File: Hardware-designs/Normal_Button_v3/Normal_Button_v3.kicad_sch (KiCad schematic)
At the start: 40 parts, among them J1 UART, J2 Bat, J3 USB_C, Q1 MMBT3904, SW1 main, SW2 Aux, SW3 Side 1, SW4 Side 2, U1 ESP32-WROOM-32, U2 TP4057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

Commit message: Add pcb images, step file, and pdf schematic for all hardware designs.
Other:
- title: (none) -> HueMix-Link Normal Button
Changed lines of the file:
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@@
 	(generator_version "9.0")
 	(paper "A4")
+	(title_block
+		(title "HueMix-Link Normal Button")
+		(date "2026-02-18")
+		(rev "3.0")
+	)
 	(junction
 		(at 187.96 26.67)

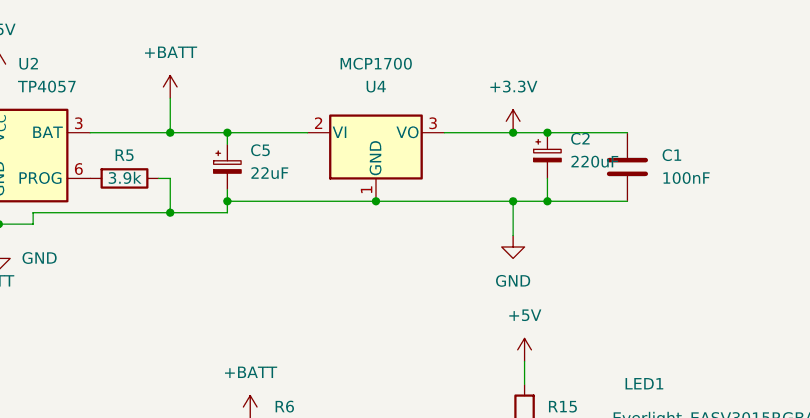
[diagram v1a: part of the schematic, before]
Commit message: correction voltage regulator
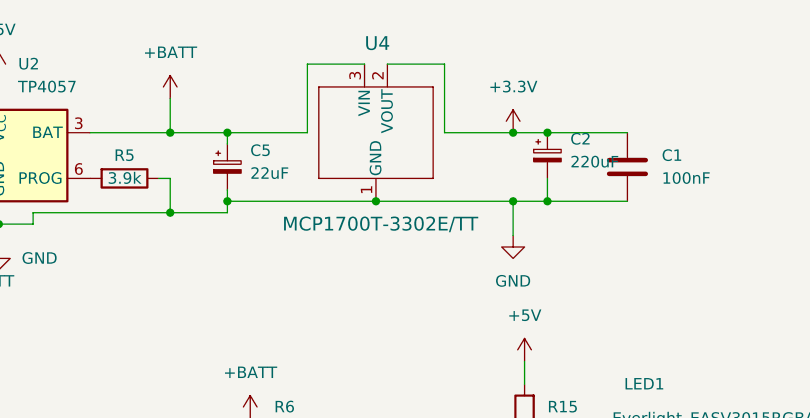
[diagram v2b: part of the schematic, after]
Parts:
- removed U4: MCP1700, MCP1700T_3302E_TT 3:SOT-23_MC_MCH, symbol Regulator_Linear:MCP1700-3302E_TO92
- added U4: MCP1700T-3302E/TT, SOT-23_MC_MCH, symbol 2025-12-22_17-16-21:MCP1700T-3302E_TT
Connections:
- net +3.3V: now also U4.2 (VOUT)
- net +BATT: now also U4.3 (VIN)
- net GND: now also U4.1 (GND)

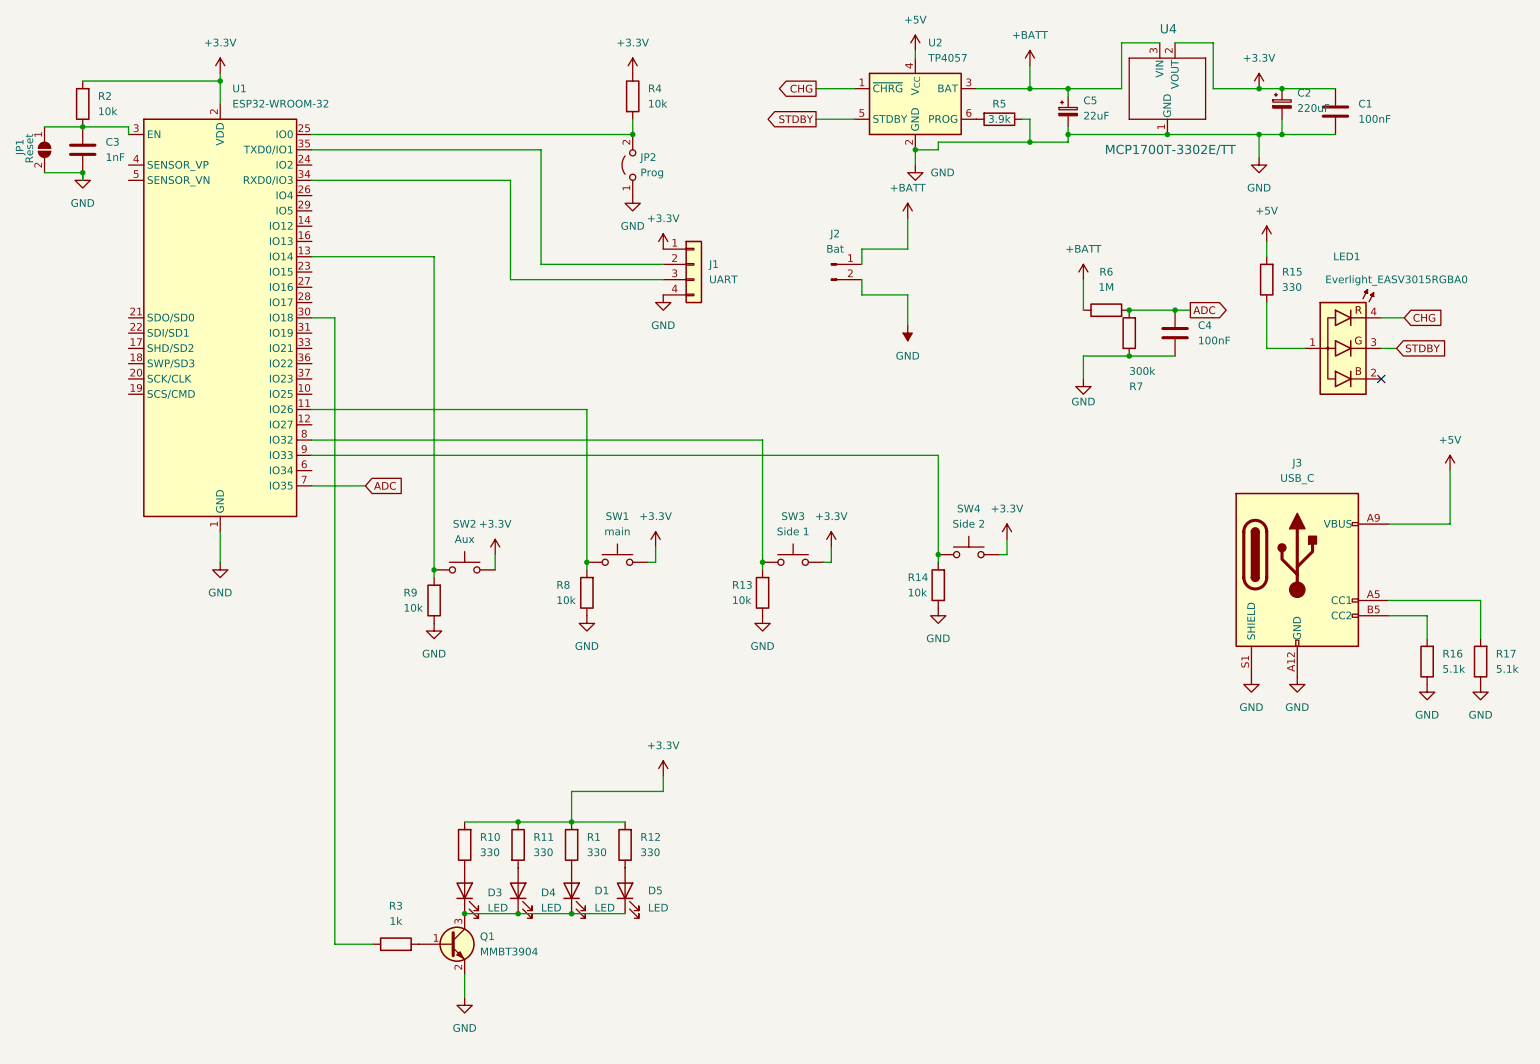
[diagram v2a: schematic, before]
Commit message: correction voltage regulator
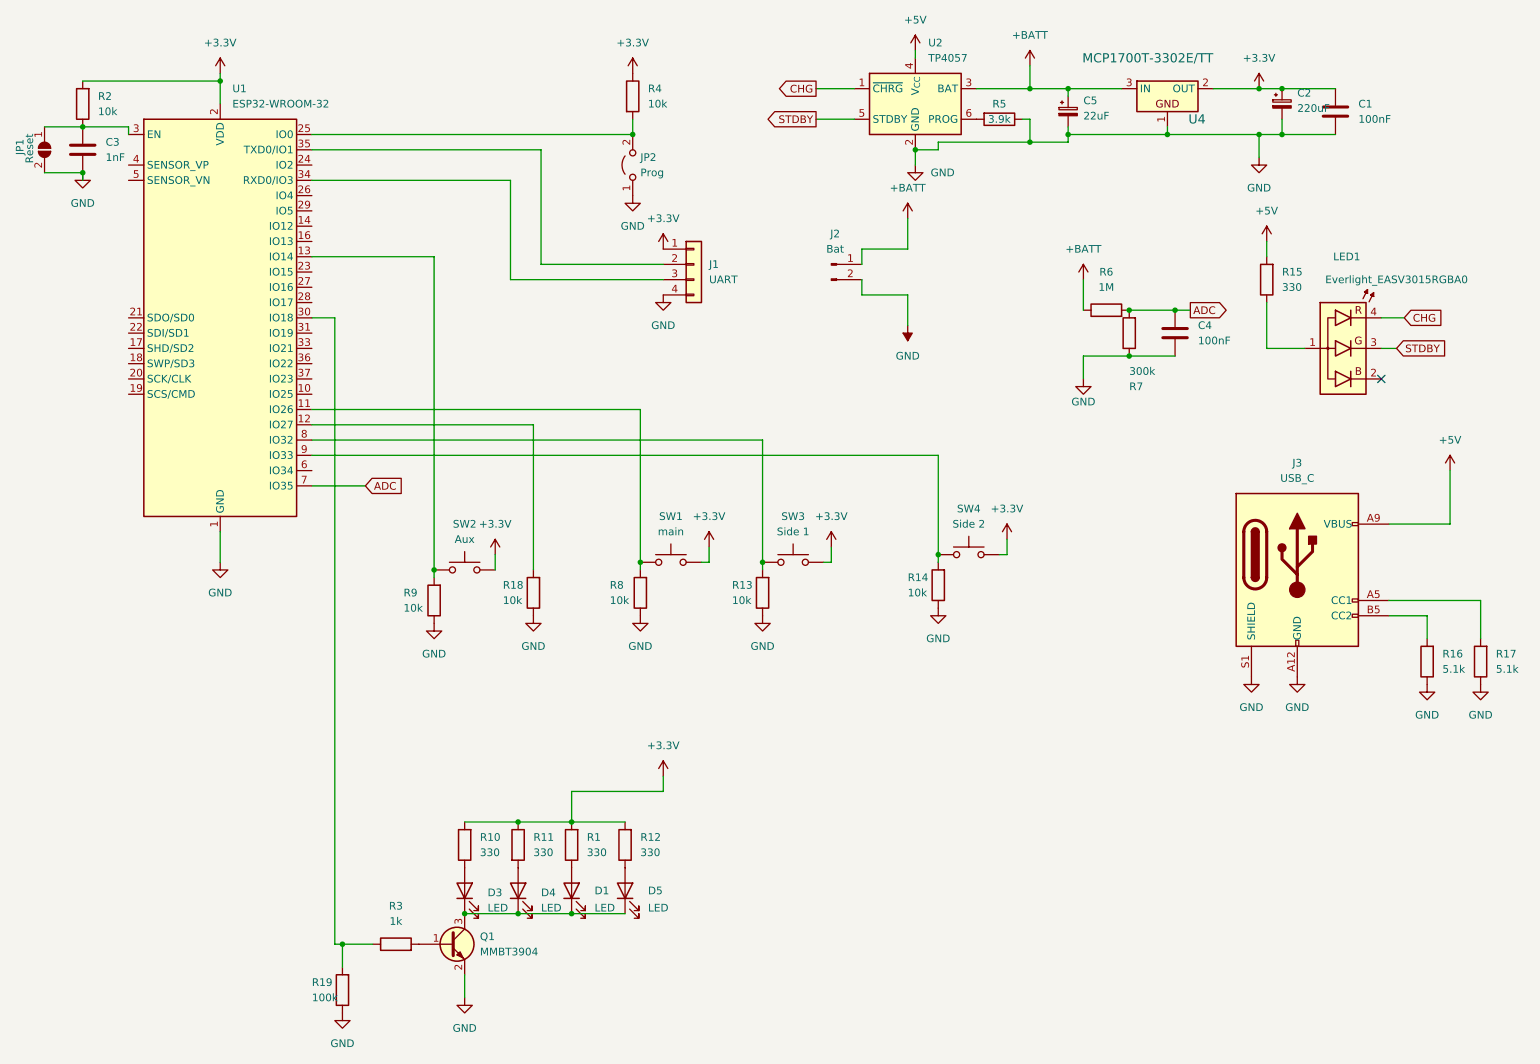
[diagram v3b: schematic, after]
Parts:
- added R18: 10k, Resistor_SMD:R_1206_3216Metric_Pad1.30x1.75mm_HandSolder, symbol Device:R
- added R19: 100k, Resistor_SMD:R_1206_3216Metric_Pad1.30x1.75mm_HandSolder, symbol Device:R
- U4: footprint SOT-23_MC_MCH -> PCM_Package_TO_SOT_SMD_AKL:SOT-23; symbol 2025-12-22_17-16-21:MCP1700T-3302E_TT -> PCM_Voltage_Regulator_AKL:MCP1700T-3302E-TT
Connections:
- net GND: now also R18.1, R19.1
- net at U1.12 (IO27): now also R18.2
- net at R3.1, U1.30 (IO18): now also R19.2
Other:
- moved on the sheet: R8, SW1

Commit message: Minor KiCad files update for all devices
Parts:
- C3: value 1nF -> 68nF
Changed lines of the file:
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@@
 			)
 		)
-		(property "Value" "1nF"
+		(property "Value" "68nF"
 			(at 27.94 38.0999 0)
 			(effects
